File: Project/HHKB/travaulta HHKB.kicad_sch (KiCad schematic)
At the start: 27 parts, among them J5 ARGB, SW38 BOOT0, U1 STM32F401CBUx, U2 XC6206PxxxMR, Y1 8 MHz

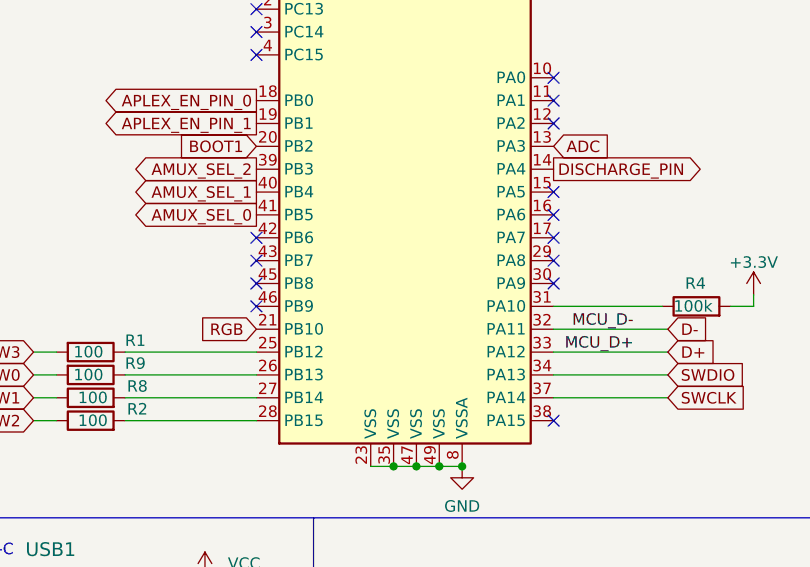
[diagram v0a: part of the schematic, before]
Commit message: changed rgb pin on HHKB&WKL for better compatibility
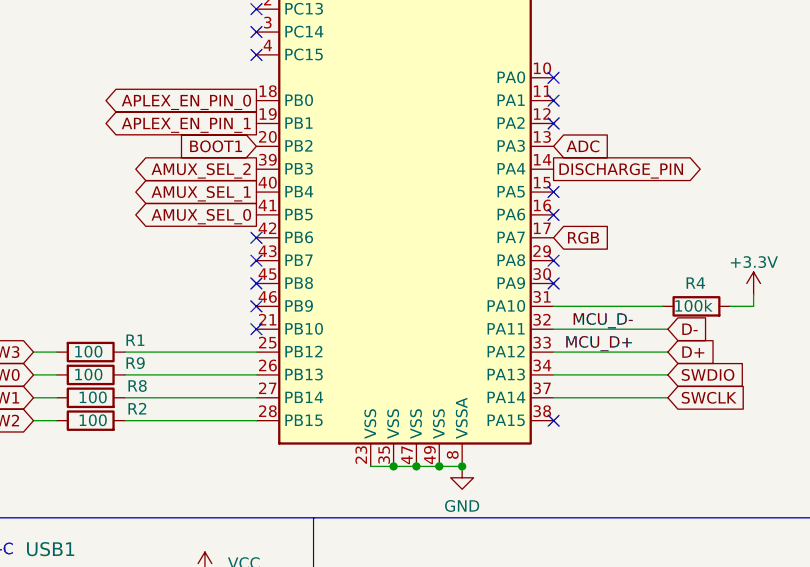
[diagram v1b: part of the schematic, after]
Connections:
- net RGB: now also U1.17 (PA7); no longer U1.21 (PB10)
